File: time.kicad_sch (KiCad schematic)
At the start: 13 parts, among them J10 Conn_01x04_Socket, J11 Conn_01x04_Socket, J9 Conn_01x04_Socket, Y1 32.768k

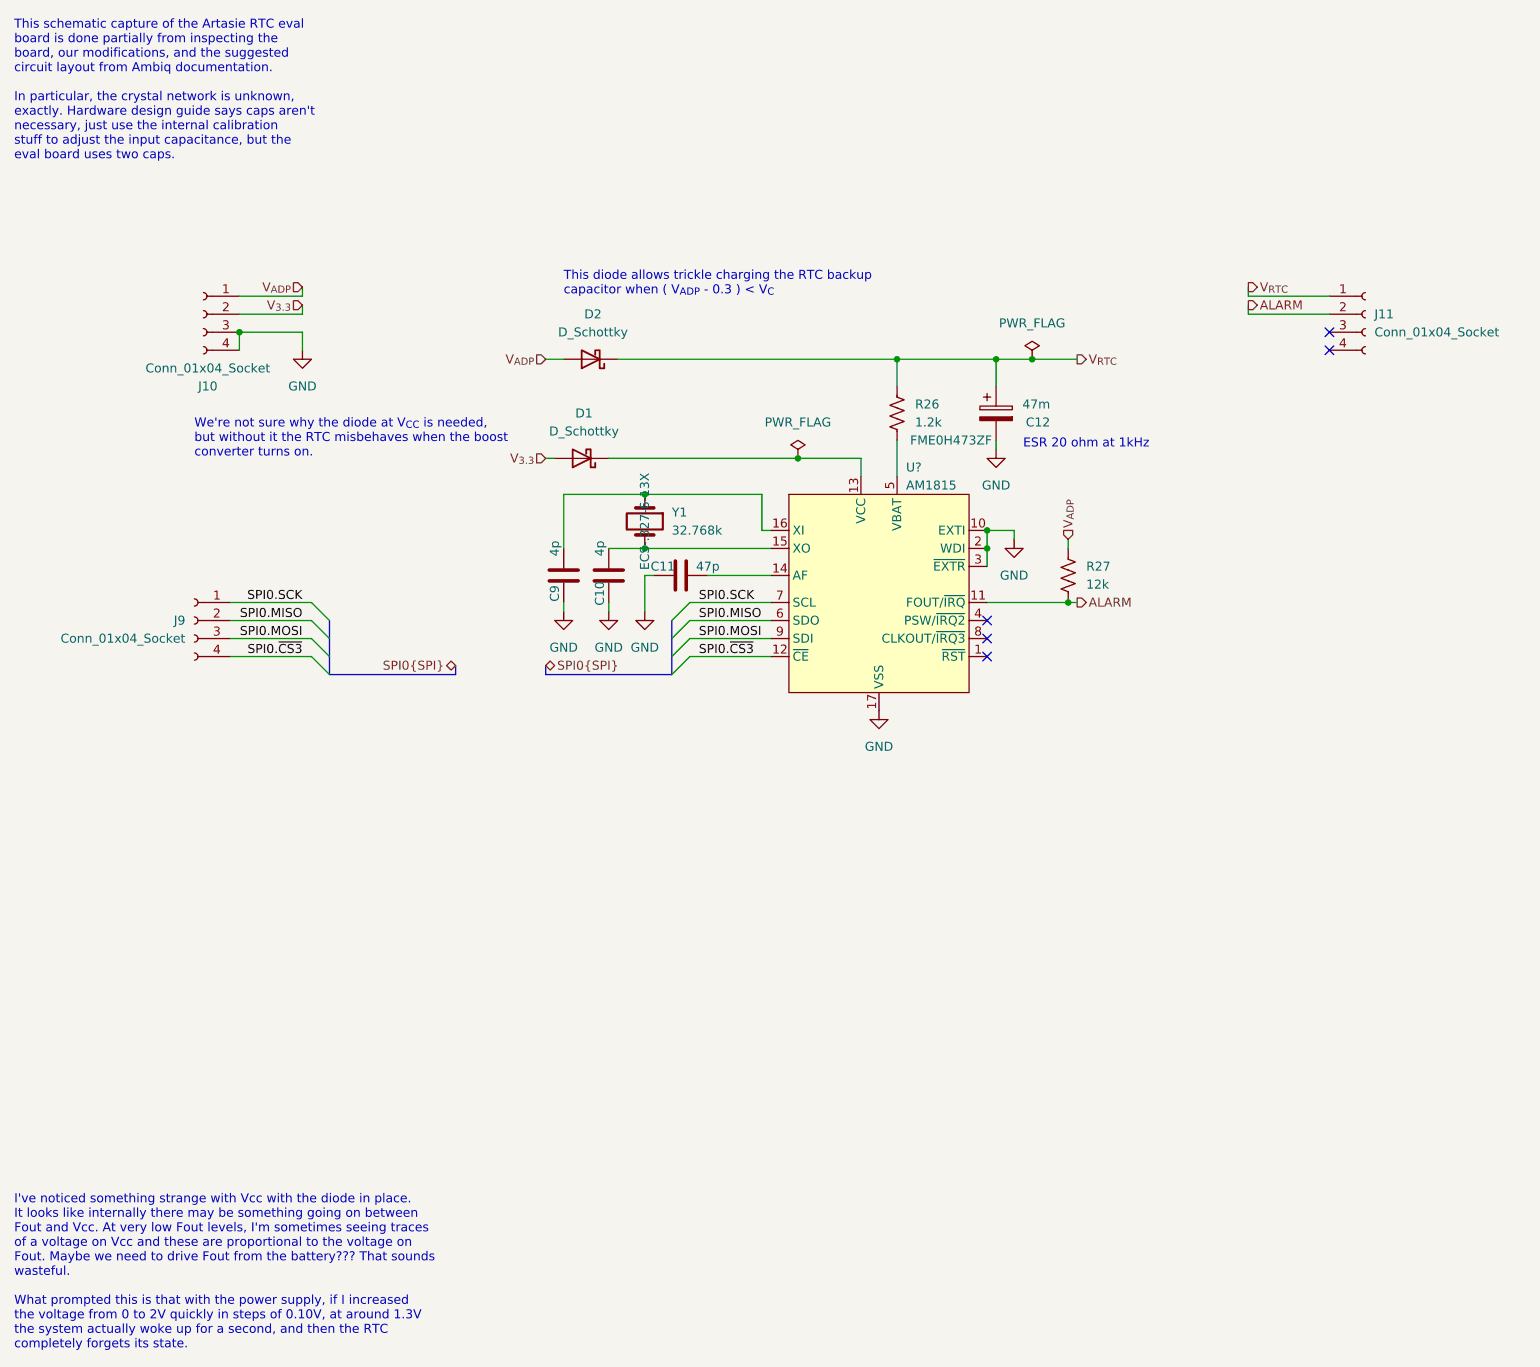
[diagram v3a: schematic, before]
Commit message: Added LoRa module, lots of fixes & tweaks
 - Added loRa module as last Artemia experiment uses LoRa RFM95W
 - Added headers for debuggging purposes
 - Expanded board size to account for added hardware
 - Updated clearances to match JLCPCB manufacturing capabilities (I
   figure that if JLCPCB can fab it, anyone else can)
 - Fixed DRC issues (still need to run analysis on schematic)
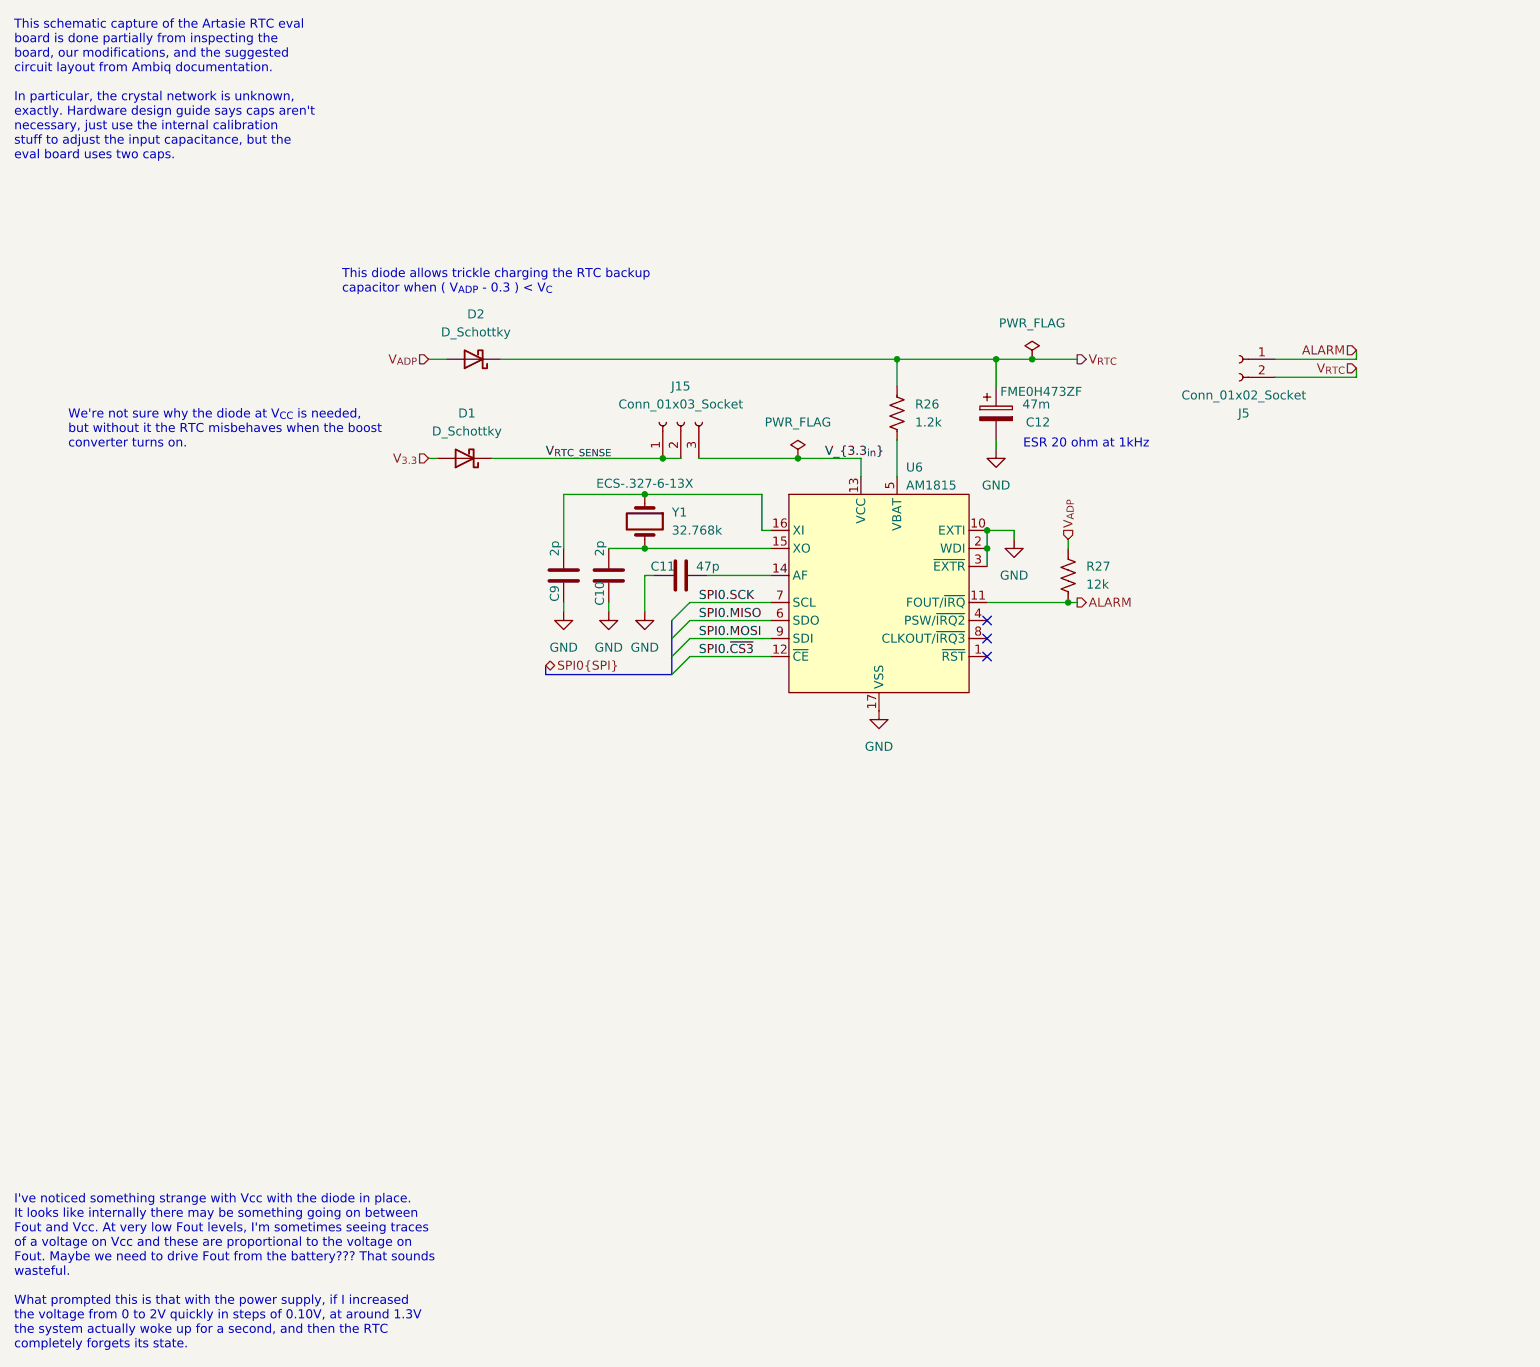
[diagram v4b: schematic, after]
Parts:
- removed J10, J11, J9: Conn_01x04_Socket, Connector_PinHeader_2.54mm:PinHeader_1x04_P2.54mm_Vertical, symbol Connector:Conn_01x04_Socket
- added J15: Conn_01x03_Socket, Connector_PinHeader_2.54mm:PinHeader_1x03_P2.54mm_Vertical, symbol Connector:Conn_01x03_Socket
- added J5: Conn_01x02_Socket, Connector_PinHeader_2.54mm:PinHeader_1x02_P2.54mm_Vertical, symbol Connector:Conn_01x02_Socket
- C10, C9: value 4p -> 2p
- C12: footprint Capacitor_THT:CP_Radial_D4.0mm_P1.50mm -> Marcano:KEMET_FM
- gave numbers to parts that had none: 1
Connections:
- net ALARM: now also J5.1 (Pin_1)
- net V_{RTC}: now also J5.2 (Pin_2)
- net V_{3.3_{in}}: now reaches U6.13 (VCC)
- net V_{3.3_{in}}: now also J15.3 (Pin_3); no longer D1.1 (K)
- new net V_{RTC_SENSE}: D1.1 (K), J15.1 (Pin_1), J15.2 (Pin_2)
- no-connect marks 5 -> 3
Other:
- title: Artemia: Time -> Artemia: Time Subsystem
- moved on the sheet: D1, D2
